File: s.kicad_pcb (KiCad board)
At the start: 2 copper layers, 200 x 75 mm, 88 parts, among them J1 USB4085-GF-A_REVB, J2 UART connector, J3 SW_PWR, J4 Conn_01x02_Pin, SW1 Z, SW10 D, SW11 S, SW12 K, SW13 W, SW14 R, SW15 STAR, SW16 R, SW17 B, SW18 G, SW19 S, SW2 T, SW20 Z, SW21 A, SW22 O, SW23 NUM, SW24 E, SW25 U, SW26 210-4MS, SW3 P, SW4 H, SW5 STAR, SW6 F, SW7 P, SW8 L, SW9 T, U1 ESP32-S3-WROOM-1, U2 MCP1825S, U3 MCP1825S, U4 AP9101CK, U5 MCP73831-2-OT, U6 DMG6968U-7, U7 DMG6968U-7

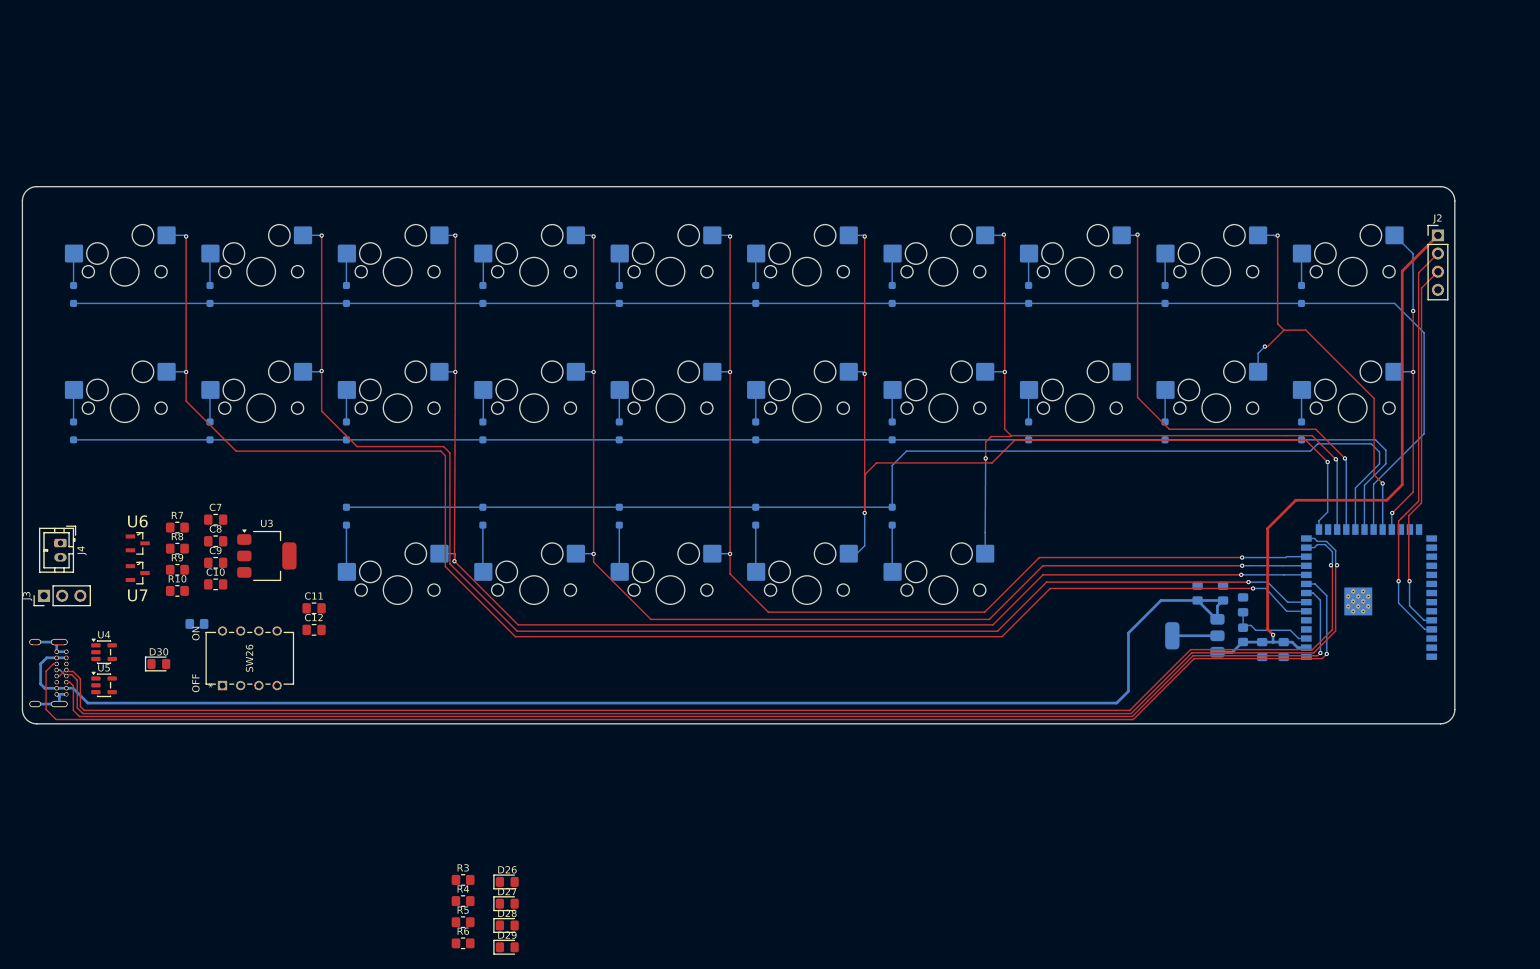
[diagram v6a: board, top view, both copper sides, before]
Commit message: route dip switches
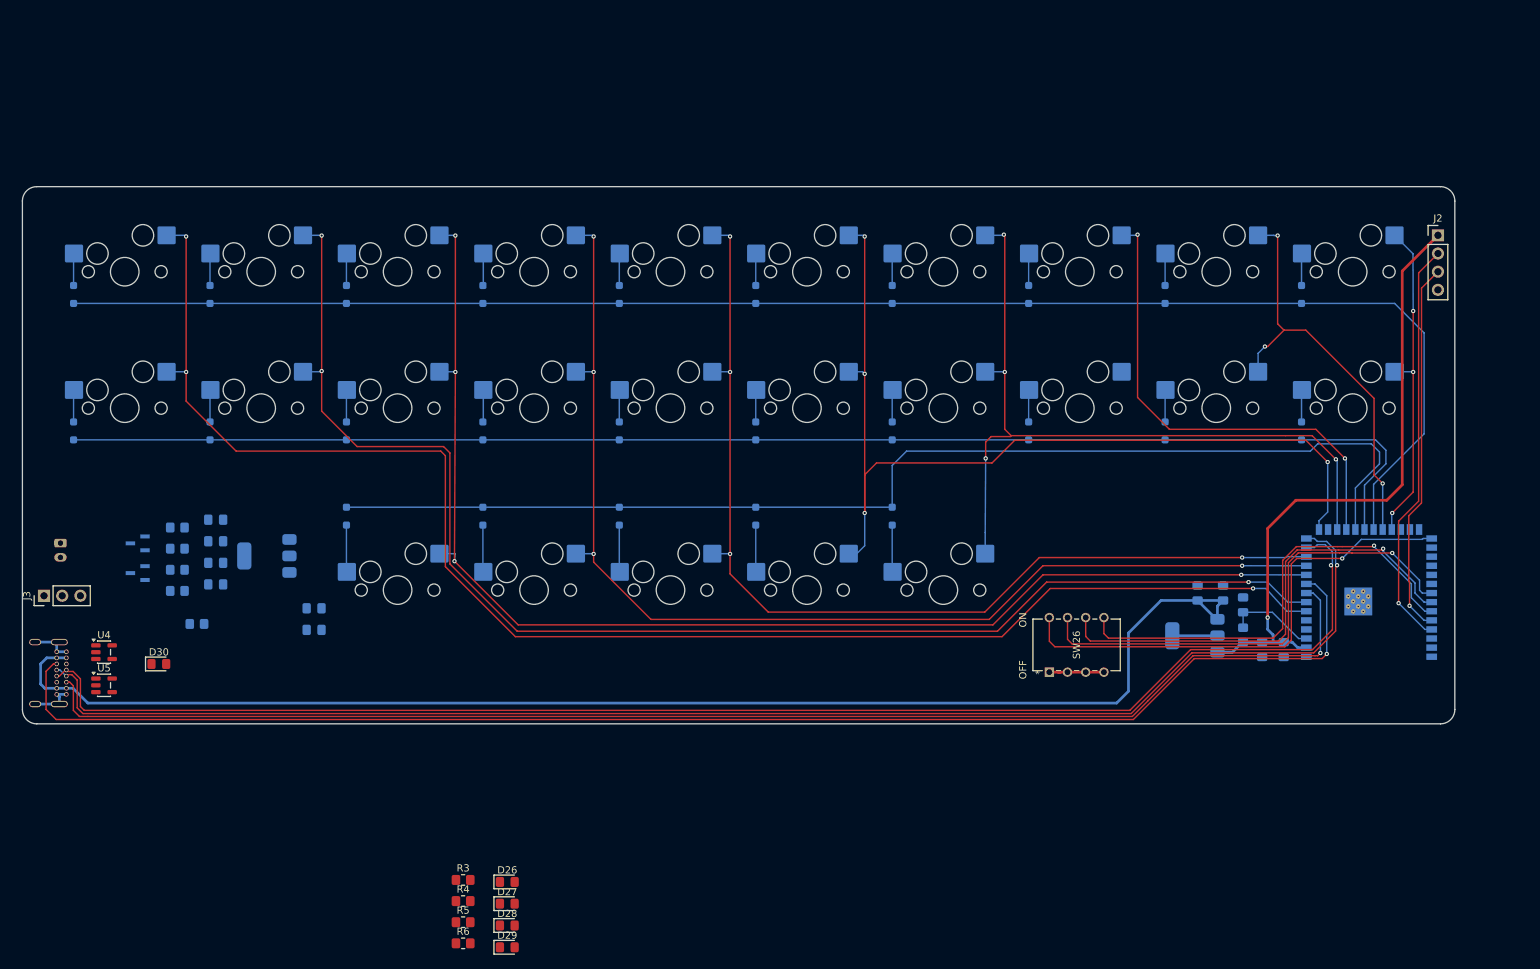
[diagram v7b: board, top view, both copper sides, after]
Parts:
- C10, C11, C12, C7, C8, C9, J4, R10, R7, R8, R9, U3, U6, U7: moved to B.Cu
- moved SW26 115.5 mm to (194.2, 131.3)
- turned C10 to 180 degrees
- turned C11 to 180 degrees
- turned C12 to 180 degrees
- turned C7 to 180 degrees
- turned C8 to 180 degrees
- turned C9 to 180 degrees
- turned R10 to 180 degrees
- turned R7 to 180 degrees
- turned R8 to 180 degrees
- turned R9 to 180 degrees
- turned U3 to 180 degrees
- turned U6 to 180 degrees
- turned U7 to 180 degrees
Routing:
- net Net-(U1-IO0): track 0.00 -> 69.5 mm, vias 0 -> 1
- net /sw_2: track 0.00 -> 68.7 mm, vias 0 -> 1
- net /sw_3: track 0.00 -> 66.6 mm, vias 0 -> 1
- net /sw_4: track 0.00 -> 64.1 mm, vias 0 -> 1
- net GND: track 18.8 -> 26.6 mm
- net Net-(U1-EN): track 12.6 -> 13.7 mm

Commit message: route battery charging stuff
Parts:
- U4, U5: moved to B.Cu
- moved R2 119.1 mm to (194.2, 120.0), turned to -90 degrees
- moved C12 29.7 mm to (62.9, 133.3), turned to 90 degrees
- moved C11 23.8 mm to (67.7, 122.6), turned to 0 degrees
- moved R7 14.8 mm to (63.1, 122.6), turned to 0 degrees
- moved C7 14.6 mm to (86.6, 121.6), turned to 0 degrees
- moved R10 14.2 mm to (82.0, 130.4), turned to -90 degrees
- moved U4 11.2 mm to (65.0, 117.7), turned to 90 degrees
- moved C8 10.8 mm to (86.8, 119.0), turned to 0 degrees
- moved C10 10.1 mm to (86.6, 114.3), turned to 0 degrees
- moved R9 9.25 mm to (71.6, 126.2), turned to 0 degrees
- moved C9 8.14 mm to (83.7, 110.5), turned to 90 degrees
- moved U7 8.07 mm to (73.3, 122.4)
- moved U6 6.99 mm to (70.6, 119.3), turned to 0 degrees
- moved D30 6.84 mm to (75.7, 133.7), turned to 180 degrees
- moved U5 6.55 mm to (64.8, 127.1)
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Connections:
- net Net-(J3-Pin_3) renamed /battery_mgmt/batt_pos
- net Net-(J4-Pin_2) renamed /battery_mgmt/batt_neg
- net Net-(U6-D) renamed /battery_mgmt/between_mosfets
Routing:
- net +3.3V: track 87.7 -> 256.2 mm, vias 1 -> 2
- net /battery_mgmt/HV_CHR: track 0.00 -> 45.3 mm
- net /battery_mgmt/batt_neg: track 0.00 -> 25.6 mm, vias 0 -> 1
- net /battery_mgmt/batt_pos: track 0.00 -> 21.4 mm
- net Net-(U5-STAT): track 0.00 -> 19.6 mm
- net /VBUS: track 190.5 -> 208.8 mm, vias 0 -> 2
- net Net-(U4-VDD): track 0.00 -> 15.2 mm
- net Net-(U4-CO): track 0.00 -> 12.0 mm, vias 0 -> 2
- net Net-(U4-DO): track 0.00 -> 8.28 mm, vias 0 -> 2
- net Net-(U4-VM): track 0.00 -> 7.51 mm
- net Net-(D30-K): track 0.00 -> 6.66 mm, vias 0 -> 1
- net Net-(U5-PROG): track 0.00 -> 5.48 mm
- net /battery_mgmt/between_mosfets: track 0.00 -> 3.44 mm
- net Net-(U1-IO0): track 69.5 -> 72.2 mm
